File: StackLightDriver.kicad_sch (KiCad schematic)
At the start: 66 parts, among them J1 B2B-XH-A, J10 B2B-XH-A, J11 PJ-102AH, J12 USB_C_Receptacle_USB2.0_14P, J2 B2B-XH-A, J3 B2B-XH-A, J4 B2B-XH-A, J5 B2B-XH-A, J6 B2B-XH-A, J7 B2B-XH-A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

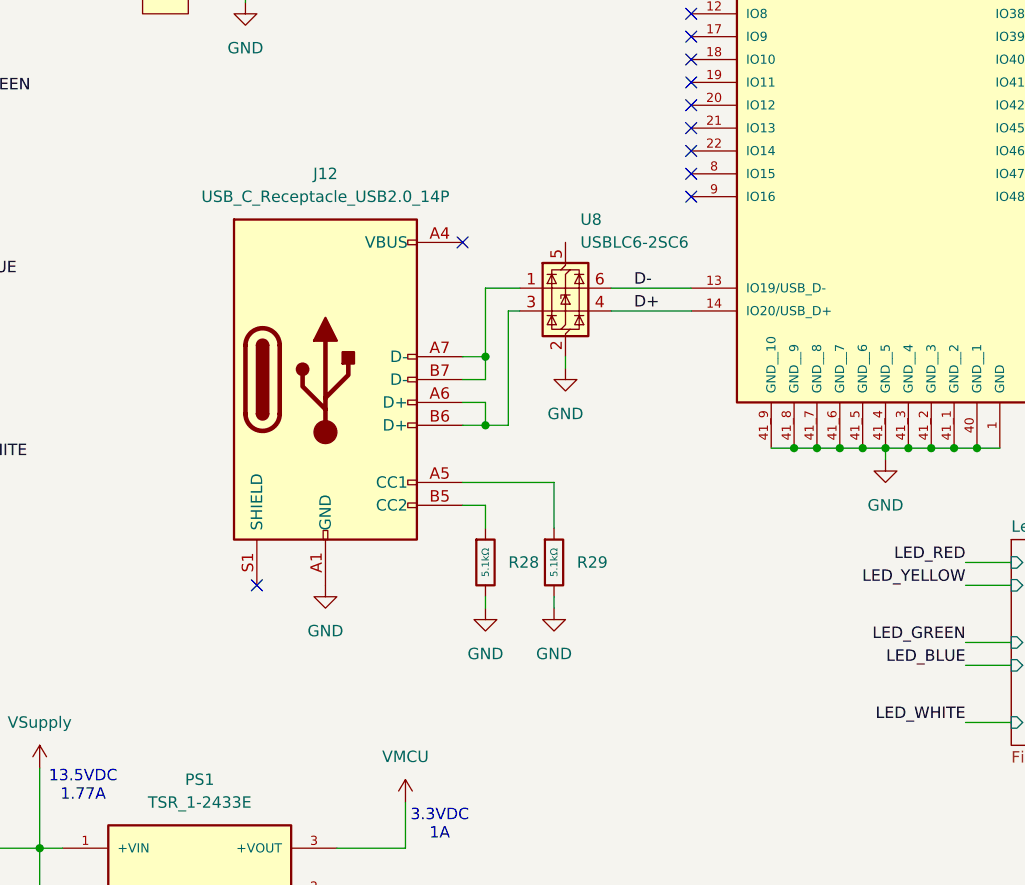
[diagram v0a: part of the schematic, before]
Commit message: Updated USB C connector schematic symbol and added voltage divider
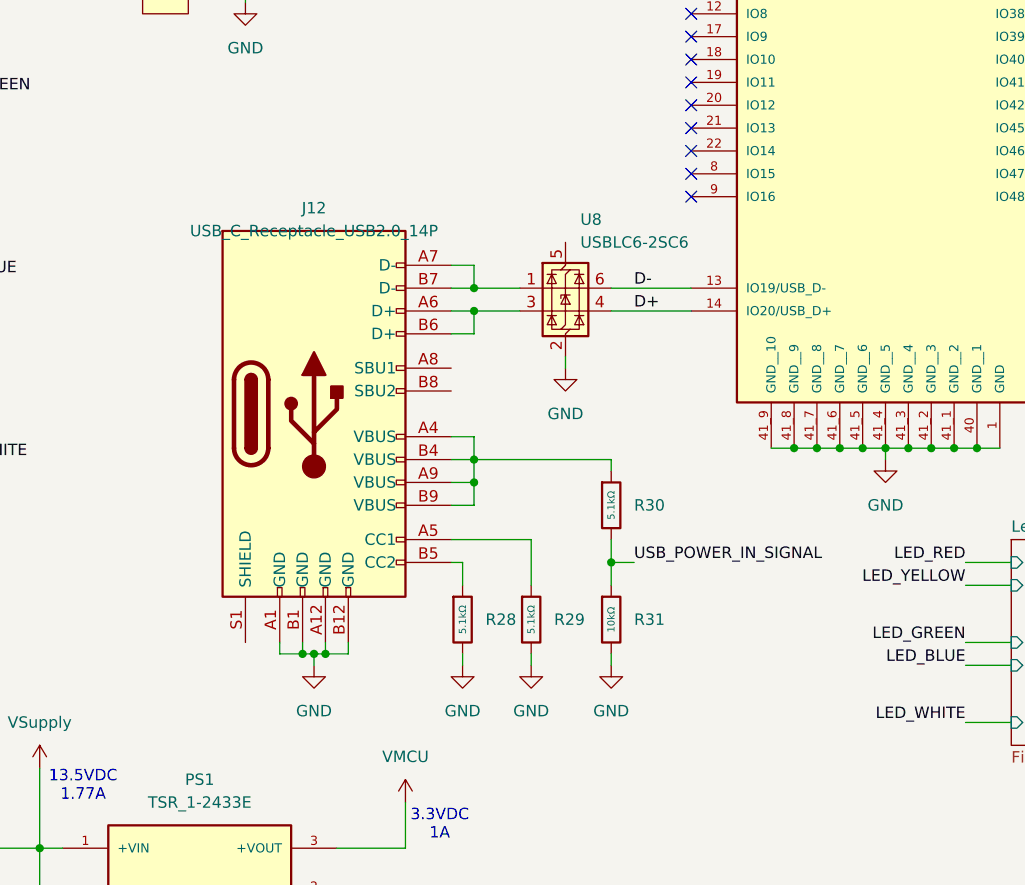
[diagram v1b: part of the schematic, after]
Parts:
- added R30: 5.1kΩ, PCM_JLCPCB:R_0805, symbol PCM_JLCPCB-Resistors:0805,5.1kΩ
- added R31: 10kΩ, PCM_JLCPCB:R_0805, symbol PCM_JLCPCB-Resistors:0805,10kΩ
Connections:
- net GND: now also R31.2
- net at J12.A4 (VBUS), J12.A9 (VBUS), J12.B4 (VBUS)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: now also R30.1
- new net USB_POWER_IN_SIGNAL: R30.2, R31.1
- no-connect marks 35 -> 33
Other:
- moved on the sheet: R28, R29

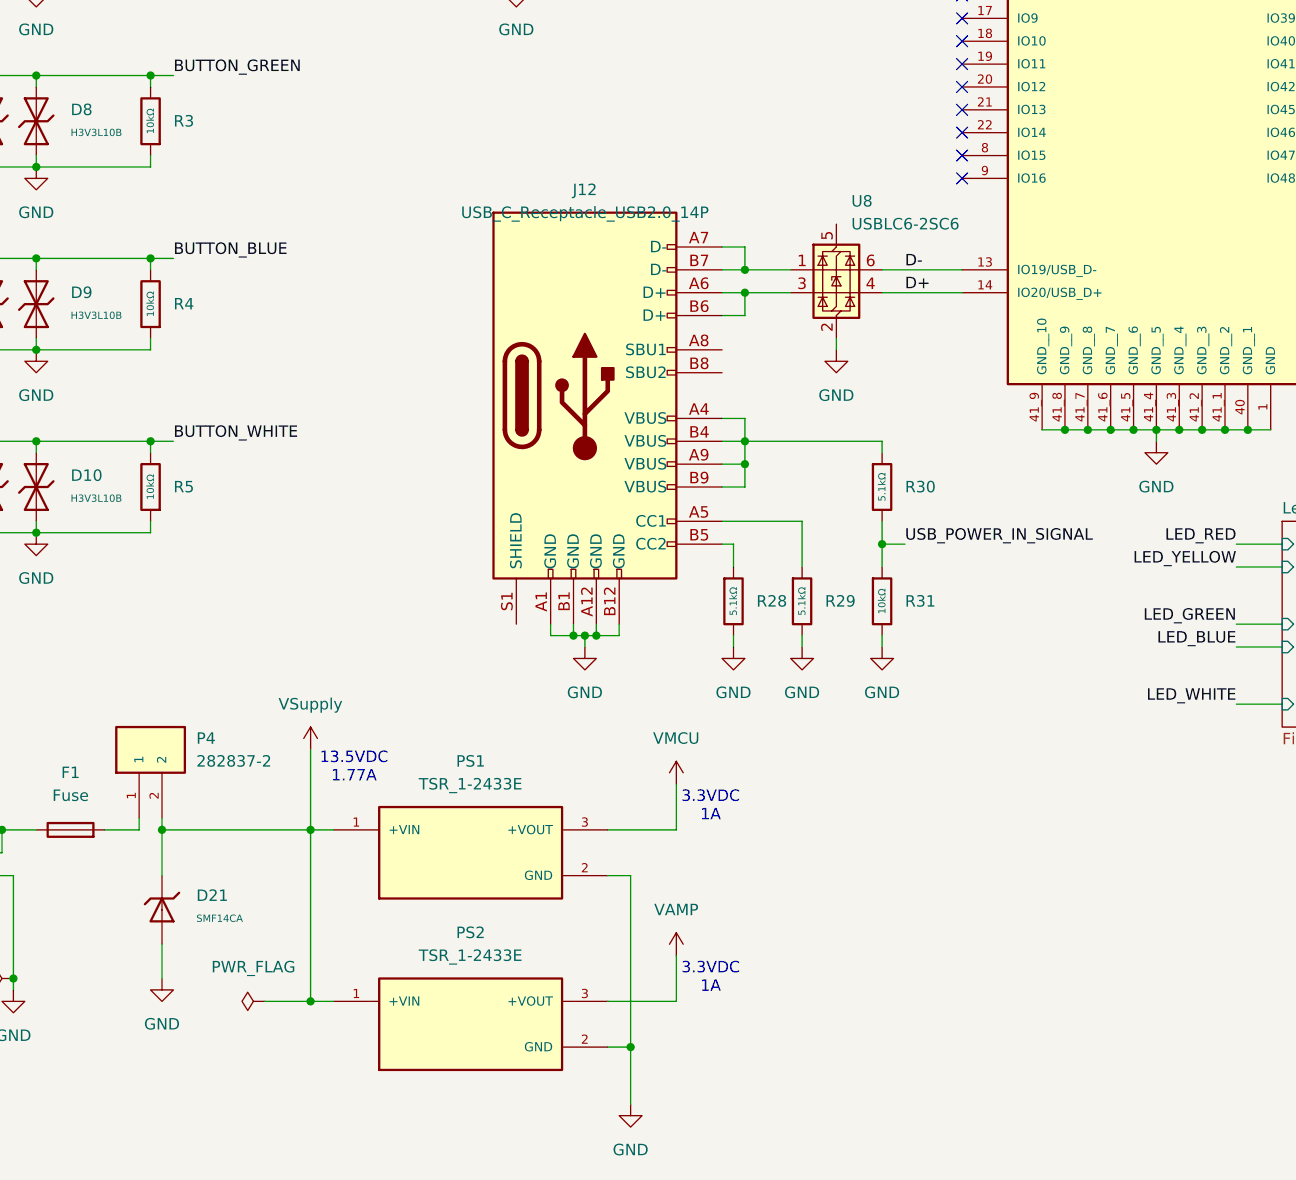
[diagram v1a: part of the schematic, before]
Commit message: Added reverse polarity mosfet
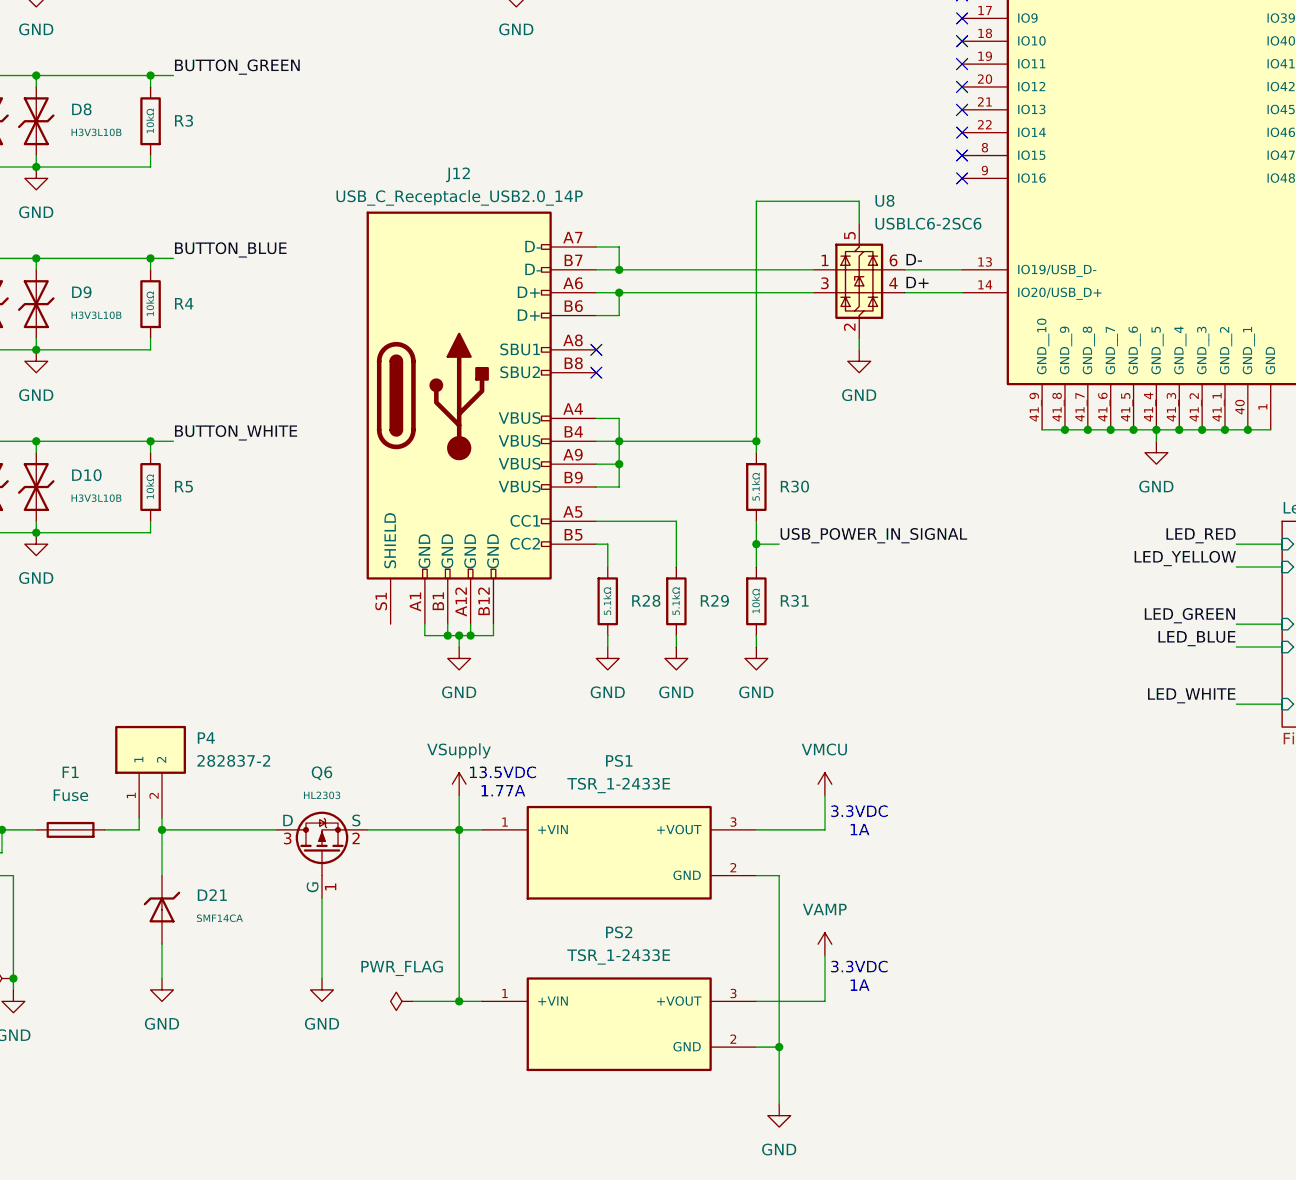
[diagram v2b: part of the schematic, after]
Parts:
- added Q6: HL2303, PCM_JLCPCB:Q_SOT-23, symbol PCM_JLCPCB-Transistors:PMOS,HL2303
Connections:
- net GND: now also Q6.1 (G)
- net VSupply: now also Q6.2 (S); no longer D21.1, P4.2
- net at J12.A4 (VBUS), J12.A9 (VBUS), J12.B4 (VBUS)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: now also U8.5 (VBUS)
- new net: D21.1, P4.2, Q6.3 (D)
- no-connect marks 33 -> 35
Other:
- moved on the sheet: J12, PS1, PS2, R28, R29, R30, R31, U8

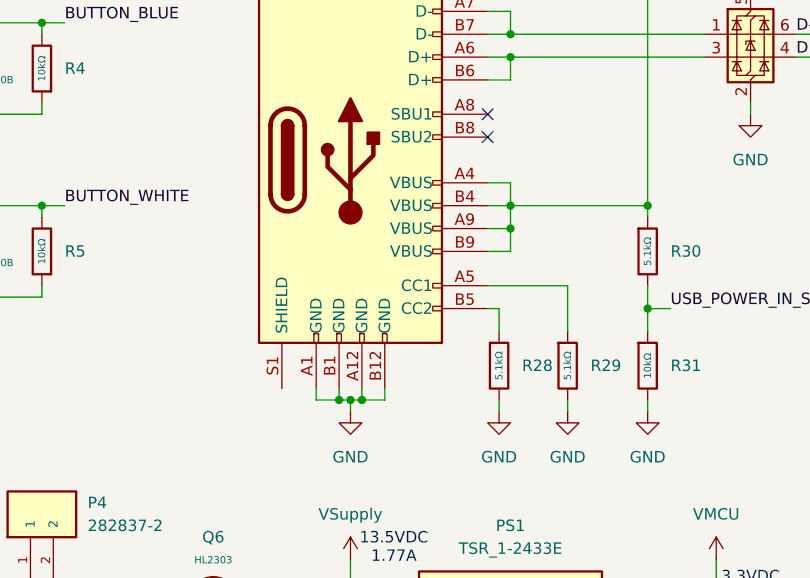
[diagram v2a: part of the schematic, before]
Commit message: Added footprint for USB-C receptacle
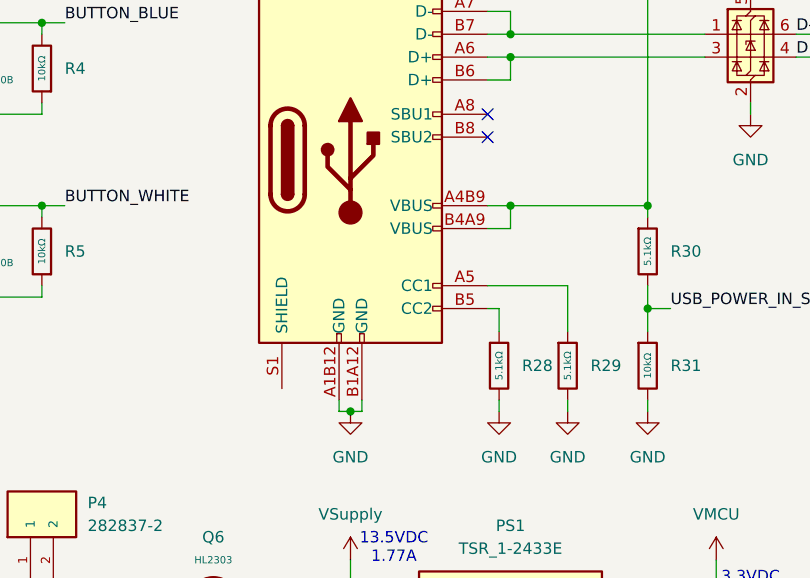
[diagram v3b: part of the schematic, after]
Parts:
- J12: footprint (none) -> Project_footprints:USB_C_Receptacle_USB2.0_14P
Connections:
- net GND: now also J12.A1B12 (GND), J12.B1A12 (GND); no longer J12.A1 (GND), J12.A12 (GND), J12.B1 (GND), J12.B12 (GND)
- new net: J12.A4B9 (VBUS), J12.B4A9 (VBUS), R30.1, U8.5 (VBUS)
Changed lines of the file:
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@@
 	)
 	(junction
-		(at 95.25 137.16)
-		(diameter 0)
-		(color 0 0 0 0)
-	)
-	(junction
 		(at 177.8 114.3)
 		(diameter 0)
@@
 	)
 	(junction
-		(at 96.52 137.16)
-		(diameter 0)
-		(color 0 0 0 0)
-	)
-	(junction
 		(at 182.88 114.3)
 		(diameter 0)
@@
 	)
 	(junction
-		(at 113.03 118.11)
-		(diameter 0)
-		(color 0 0 0 0)
-	)
-	(junction
 		(at 33.02 31.75)
 		(diameter 0)
@@
 	)
 	(junction
+		(at 95.25 138.43)
+		(diameter 0)
+		(color 0 0 0 0)
+	)
+	(junction
 		(at 266.7 78.74)
 		(diameter 0)
@@
 	)
 	(junction
-		(at 93.98 137.16)
-		(diameter 0)
-		(color 0 0 0 0)
-	)
-	(junction
 		(at 232.41 161.29)
 		(diameter 0)
@@
 	(wire
 		(pts
-			(xy 95.25 137.16) (xy 95.25 138.43)
-		)
-		(stroke
-			(width 0)
-			(type default)
-		)
-	)
-	(wire
-		(pts
 			(xy 33.02 31.75) (xy 33.02 27.94)
 		)
@@
 	(wire
 		(pts
-			(xy 110.49 120.65) (xy 113.03 120.65)
-		)
-		(stroke
-			(width 0)
-			(type default)
-		)
-	)
-	(wire
-		(pts
 			(xy 33.02 113.03) (xy 43.18 113.03)
 		)
@@
 	(wire
 		(pts
-			(xy 113.03 118.11) (xy 113.03 120.65)
-		)
-		(stroke
-			(width 0)
-			(type default)
-		)
-	)
-	(wire
-		(pts
 			(xy 218.44 153.67) (xy 218.44 161.29)
 		)
@@
 	(wire
 		(pts
-			(xy 96.52 135.89) (xy 96.52 137.16)
-		)
-		(stroke
-			(width 0)
-			(type default)
-		)
-	)
-	(wire
-		(pts
 			(xy 48.26 64.77) (xy 60.96 64.77)
 		)
@@
 	(wire
 		(pts
-			(xy 93.98 137.16) (xy 95.25 137.16)
-		)
-		(stroke
-			(width 0)
-			(type default)
-		)
-	)
-	(wire
-		(pts
 			(xy 175.26 114.3) (xy 177.8 114.3)
 		)
@@
 	(wire
 		(pts
-			(xy 96.52 137.16) (xy 99.06 137.16)
-		)
-		(stroke
-			(width 0)
-			(type default)
-		)
-	)
-	(wire
-		(pts
 			(xy 238.76 76.2) (xy 241.3 76.2)
 		)
@@
 	(wire
 		(pts
-			(xy 91.44 135.89) (xy 91.44 137.16)
-		)
-		(stroke
-			(width 0)
-			(type default)
-		)
-	)
-	(wire
-		(pts
 			(xy 260.35 102.87) (xy 260.35 104.14)
 		)
@@
 	(wire
 		(pts
+			(xy 93.98 137.16) (xy 93.98 138.43)
+		)
+		(stroke
+			(width 0)
+			(type default)
+		)
+	)
+	(wire
+		(pts
 			(xy 48.26 95.25) (xy 60.96 95.25)
 		)
@@
 	(wire
 		(pts
-			(xy 113.03 115.57) (xy 113.03 113.03)
-		)
-		(stroke
-			(width 0)
-			(type default)
-		)
-	)
-	(wire
-		(pts
 			(xy 43.18 43.18) (xy 43.18 44.45)
 		)
@@
 	(wire
 		(pts
-			(xy 99.06 137.16) (xy 99.06 135.89)
-		)
-		(stroke
-			(width 0)
-			(type default)
-		)
-	)
-	(wire
-		(pts
 			(xy 48.26 85.09) (xy 60.96 85.09)
 		)
@@
 	(wire
 		(pts
+			(xy 93.98 138.43) (xy 95.25 138.43)
+		)
+		(stroke
+			(width 0)
+			(type default)
+		)
+	)
+	(wire
+		(pts
 			(xy 219.71 105.41) (xy 229.87 105.41)
 		)
@@
 	(wire
 		(pts
+			(xy 96.52 138.43) (xy 96.52 137.16)
+		)
+		(stroke
+			(width 0)
+			(type default)
+		)
+	)
+	(wire
+		(pts
 			(xy 48.26 74.93) (xy 48.26 76.2)
 		)
@@
 	(wire
 		(pts
-			(xy 93.98 135.89) (xy 93.98 137.16)
-		)
-		(stroke
-			(width 0)
-			(type default)
-		)
-	)
-	(wire
-		(pts
-			(xy 95.25 137.16) (xy 96.52 137.16)
-		)
-		(stroke
-			(width 0)
-			(type default)
-		)
-	)
-	(wire
-		(pts
 			(xy 218.44 144.78) (xy 261.62 144.78)
 		)
@@
 	(wire
 		(pts
-			(xy 232.41 135.89) (xy 232.41 146.05)
+			(xy 95.25 138.43) (xy 96.52 138.43)
 		)
 		(stroke
@@
 	(wire
 		(pts
-			(xy 45.72 163.83) (xy 45.72 175.26)
+			(xy 232.41 135.89) (xy 232.41 146.05)
 		)
 		(stroke
@@
 	(wire
 		(pts
-			(xy 29.21 74.93) (xy 48.26 74.93)
+			(xy 45.72 163.83) (xy 45.72 175.26)
 		)
 		(stroke
@@
 	(wire
 		(pts
-			(xy 91.44 137.16) (xy 93.98 137.16)
+			(xy 29.21 74.93) (xy 48.26 74.93)
 		)
 		(stroke
@@
 	(wire
 		(pts
-			(xy 110.49 113.03) (xy 113.03 113.03)
-		)
-		(stroke
-			(width 0)
-			(type default)
-		)
-	)
-	(wire
-		(pts
 			(xy 162.56 114.3) (xy 165.1 114.3)
 		)
@@
 			)
 		)
-		(property "Footprint" ""
+		(property "Footprint" "Project_footprints:USB_C_Receptacle_USB2.0_14P"
 			(at 99.06 110.49 0)
 			(effects
@@
 		(pin "S1"
 		)
-		(pin "B9"
+		(pin "A1B12"
 		)
 		(pin "A6"
 		)
-		(pin "B12"
-		)
-		(pin "B1"
-		)
-		(pin "A1"
-		)
 		(pin "A7"
 		)
-		(pin "A9"
+		(pin "A4B9"
 		)
 		(pin "B7"
@@
 		(pin "A5"
 		)
-		(pin "A4"
-		)
-		(pin "B4"
+		(pin "B1A12"
 		)
 		(pin "B5"
@@
 		(pin "B6"
 		)
-		(pin "A12"
+		(pin "B4A9"
 		)
 		(pin "B8"

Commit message: First routing attempt
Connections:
- net BCLK: now also U6.11 (IO18)
- net BUTTON_BLUE: now also U6.21 (IO13)
- net BUTTON_GREEN: now also U6.22 (IO14)
- net BUTTON_LED_BLUE: now also U6.18 (IO10)
- net BUTTON_LED_GREEN: now also U6.17 (IO9)
- net BUTTON_LED_RED: now also U6.15 (IO3)
- net BUTTON_LED_WHITE: now also U6.19 (IO11)
- net BUTTON_LED_YELLOW: now also U6.16 (IO46)
- net BUTTON_RED: now also U6.24 (IO47)
- net BUTTON_WHITE: now also U6.20 (IO12)
- net BUTTON_YELLOW: now also U6.23 (IO21)
- net DIN: now also U6.10 (IO17)
- net GND: now also U6.41_10 (GND__11), U6.41_11 (GND__12), U6.41_12 (GND__13), U6.41_13 (GND__14), U6.41_14 (GND__15), U6.41_15 (GND__16), U6.41_16 (GND__17), U6.41_17 (GND__18), U6.41_18 (GND__19), U6.41_19 (GND__20), U6.41_20 (GND__21), U6.41_21 (GND__22)
- net LED_BLUE: now also U6.8 (IO15)
- net LED_GREEN: now also U6.7 (IO7)
- net LED_RED: now also U6.5 (IO5)
- net LED_WHITE: now also U6.9 (IO16)
- net LED_YELLOW: now also U6.6 (IO6)
- net LRC: now also U6.12 (IO8)
- net USB_POWER_IN_SIGNAL: now also U6.25 (IO48)
- no-connect marks 35 -> 17
